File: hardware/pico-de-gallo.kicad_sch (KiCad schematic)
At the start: 12 parts, among them J1 Conn_02x08_Odd_Even, J2 Conn_01x02, J3 Conn_01x04, J4 Conn_01x05, J5 Conn_01x02, J6 Conn_01x03, J7 Conn_02x05_Odd_Even

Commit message: Minor updates
Signed-off-by: Felipe Balbi <febalbi@microsoft.com>
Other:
- company: (none) -> ${COMPANY}
- title: (none) -> ${PROJECT}
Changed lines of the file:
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@@
 	(generator "eeschema")
 	(generator_version "9.0")
-	(paper "A4")
+	(paper "USLetter")
+	(title_block
+		(title "${PROJECT}")
+		(date "2025-08-29")
+		(rev "${REVISION}")
+		(company "${COMPANY}")
+		(comment 1 "Designed by: ${AUTHOR}")
+		(comment 2 "https://creativecommons.org/licenses/by-sa/4.0/")
+		(comment 3 "Attribution Share-Alike 4.0 License")
+		(comment 4 "Released under the Creative Commons")
+	)
 	(no_connect
 		(at 146.05 57.15)

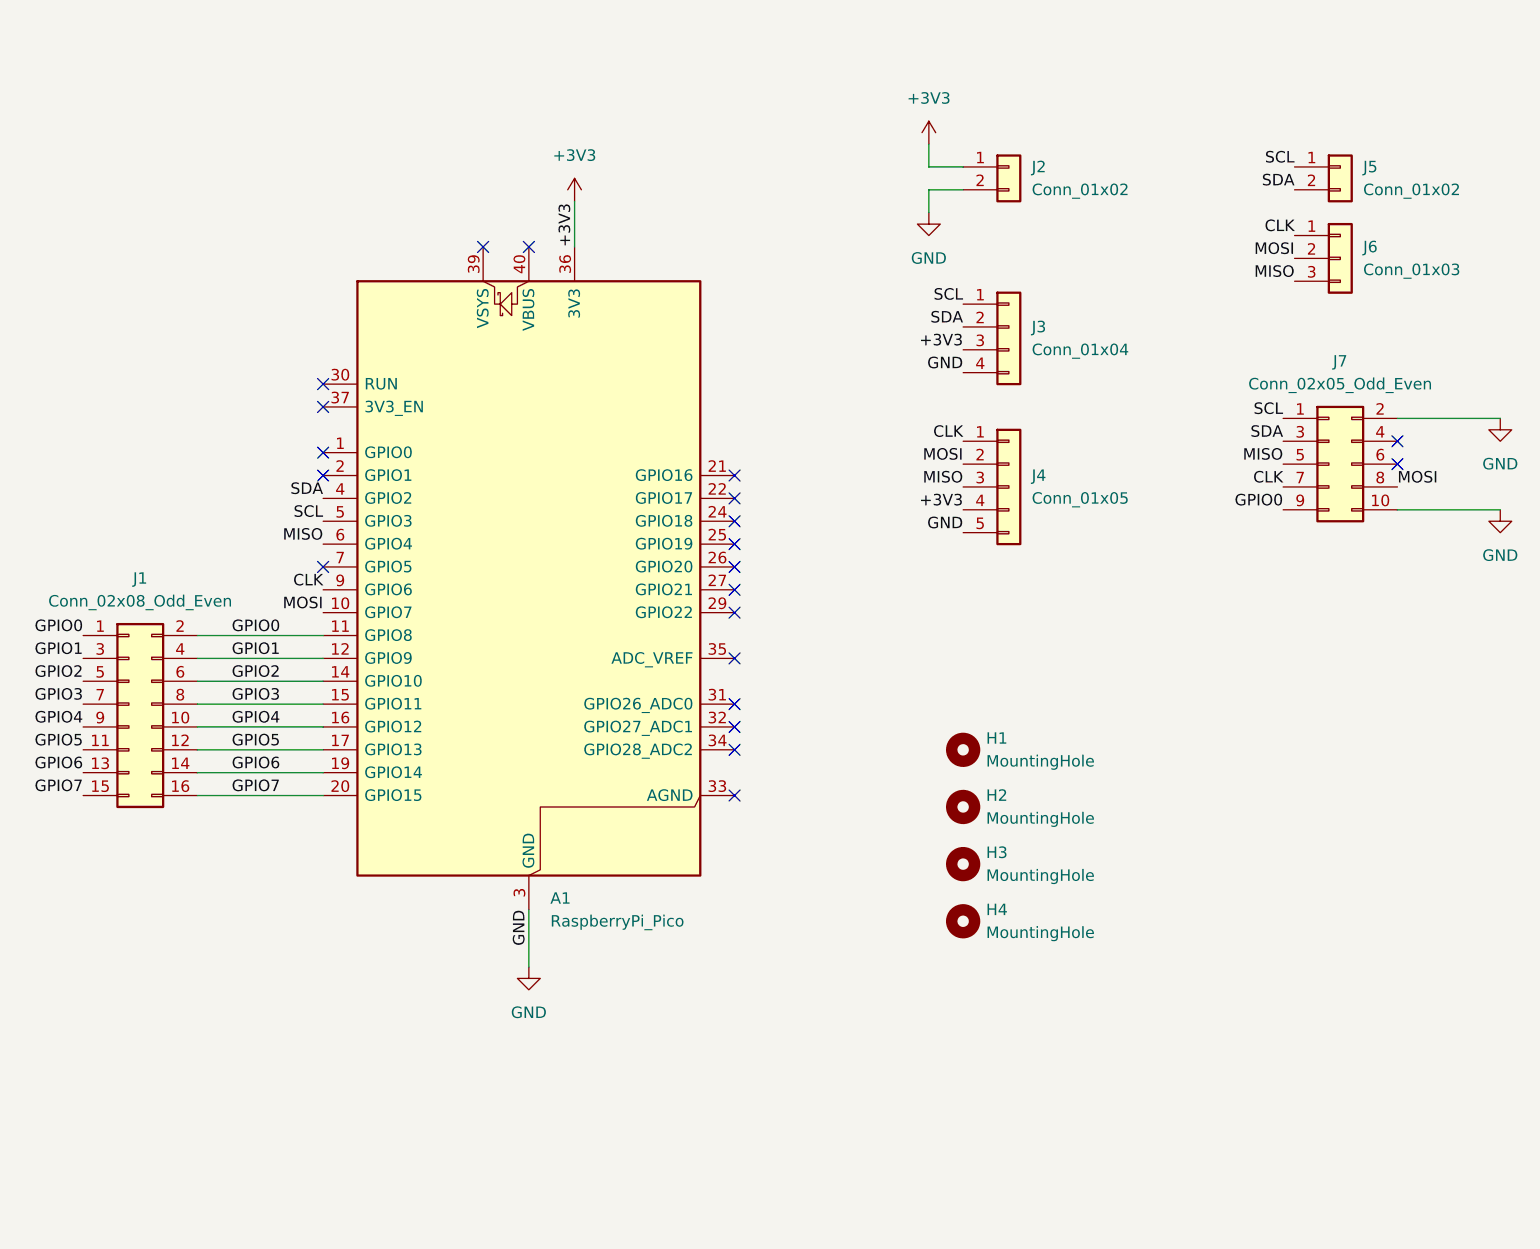
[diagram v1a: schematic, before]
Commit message: Pico de Gallo Hardware v1.1
Update the PCB for revision 1.1 of the main board.
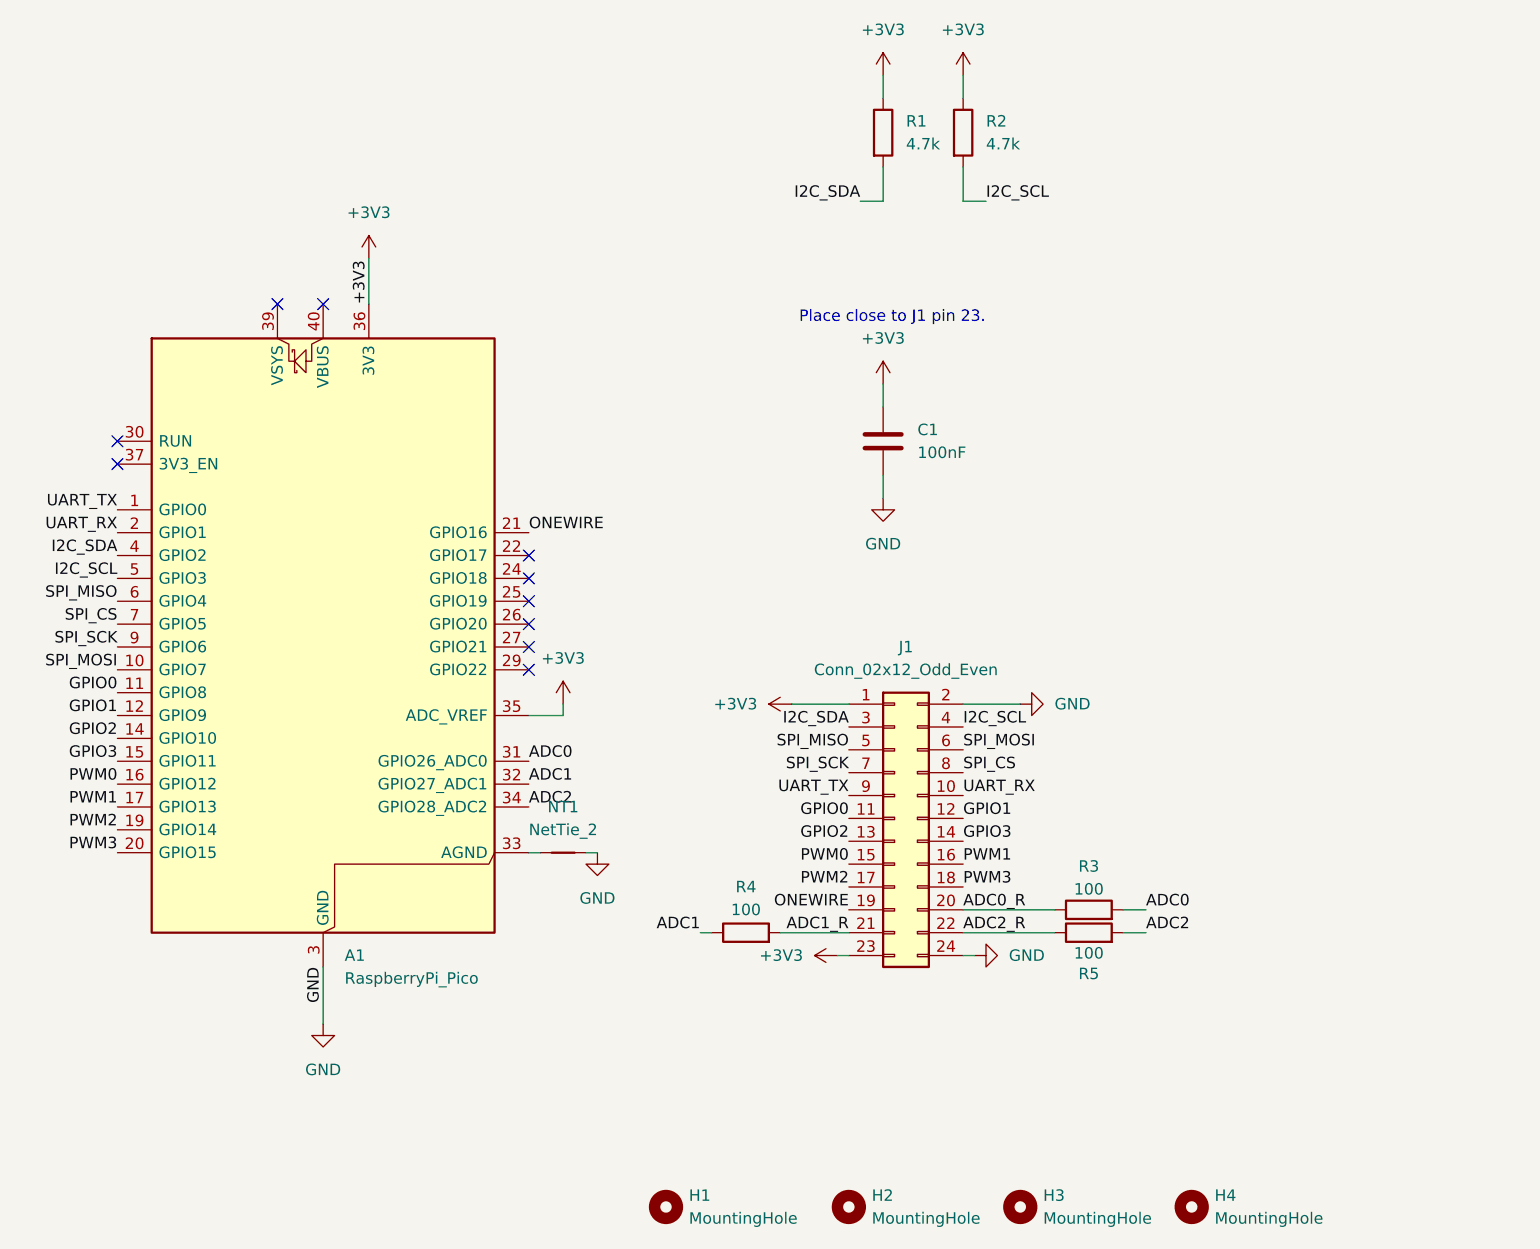
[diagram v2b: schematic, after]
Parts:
- removed J1: Conn_02x08_Odd_Even, Connector_PinHeader_2.54mm:PinHeader_2x08_P2.54mm_Vertical, symbol Connector_Generic:Conn_02x08_Odd_Even
- removed J2, J5: Conn_01x02, Connector_PinHeader_2.54mm:PinHeader_1x02_P2.54mm_Vertical, symbol Connector_Generic:Conn_01x02
- removed J3: Conn_01x04, Connector_PinSocket_2.54mm:PinSocket_1x04_P2.54mm_Horizontal, symbol Connector_Generic:Conn_01x04
- removed J4: Conn_01x05, Connector_PinSocket_2.54mm:PinSocket_1x05_P2.54mm_Horizontal, symbol Connector_Generic:Conn_01x05
- removed J6: Conn_01x03, Connector_PinHeader_2.54mm:PinHeader_1x03_P2.54mm_Vertical, symbol Connector_Generic:Conn_01x03
- removed J7: Conn_02x05_Odd_Even, Connector_PinHeader_2.54mm:PinHeader_2x05_P2.54mm_Vertical_SMD, symbol Connector_Generic:Conn_02x05_Odd_Even
- added C1: 100nF, Capacitor_SMD:C_0603_1608Metric_Pad1.08x0.95mm_HandSolder, symbol Device:C
- added J1: Conn_02x12_Odd_Even, Connector_IDC:IDC-Header_2x12_P2.54mm_Vertical, symbol Connector_Generic:Conn_02x12_Odd_Even
- added NT1: NetTie_2, NetTie:NetTie-2_SMD_Pad0.5mm, symbol Device:NetTie_2
- added R1, R2: 4.7k, Resistor_SMD:R_0603_1608Metric_Pad0.98x0.95mm_HandSolder, symbol Device:R
- added R3, R4, R5: 100, Resistor_SMD:R_0603_1608Metric_Pad0.98x0.95mm_HandSolder, symbol Device:R
- A1: now left out of the parts list
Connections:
- net +3V3: now also A1.35 (ADC_VREF), C1.1, J1.1 (Pin_1), J1.23 (Pin_23), R1.1, R2.1
- net GND: now also C1.2, J1.2 (Pin_2), J1.24 (Pin_24), NT1.2
- net GPIO0: now also J1.11 (Pin_11)
- net GPIO1: now also J1.12 (Pin_12)
- net GPIO2: now also J1.13 (Pin_13)
- net GPIO3: now also J1.14 (Pin_14)
- net UART_TX: now reaches A1.1 (GPIO0)
- net UART_TX: now also J1.9 (Pin_9)
- net UART_RX: now reaches A1.2 (GPIO1)
- net UART_RX: now also J1.10 (Pin_10)
- net ONEWIRE: now reaches A1.21 (GPIO16)
- net ONEWIRE: now also J1.19 (Pin_19)
- net ADC0: now reaches A1.31 (GPIO26_ADC0)
- net ADC0: now also R3.2
- net ADC1: now reaches A1.32 (GPIO27_ADC1)
- net ADC1: now also R4.1
- net at A1.33 (AGND): now also NT1.1
- net ADC2: now reaches A1.34 (GPIO28_ADC2)
- net ADC2: now also R5.2
- net SPI_CS: now reaches A1.7 (GPIO5)
- net SPI_CS: now also J1.8 (Pin_8)
- net CLK renamed SPI_SCK
- net SPI_SCK: now also J1.7 (Pin_7)
- net GPIO4 renamed PWM0
- net PWM0: now also J1.15 (Pin_15)
- net GPIO5 renamed PWM1
- net PWM1: now also J1.16 (Pin_16)
- net GPIO6 renamed PWM2
- net PWM2: now also J1.17 (Pin_17)
- net GPIO7 renamed PWM3
- net PWM3: now also J1.18 (Pin_18)
- net MISO renamed SPI_MISO
- net SPI_MISO: now also J1.5 (Pin_5)
- net MOSI renamed SPI_MOSI
- net SPI_MOSI: now also J1.6 (Pin_6)
- net SCL renamed I2C_SCL
- net I2C_SCL: now also J1.4 (Pin_4), R2.2
- net SDA renamed I2C_SDA
- net I2C_SDA: now also J1.3 (Pin_3), R1.2
- new net ADC0_R: J1.20 (Pin_20), R3.1
- new net ADC1_R: J1.21 (Pin_21), R4.2
- new net ADC2_R: J1.22 (Pin_22), R5.1
- no-connect marks 21 -> 10
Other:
- note added: "Place close to J1 pin 23."
- moved on the sheet: A1, H1, H2, H3, H4

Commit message: add Pico2 LCSC part number
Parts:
- A1: LCSC (none) -> C41407547; now in the parts list
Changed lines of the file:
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@@
 		(body_style 1)
 		(exclude_from_sim no)
-		(in_bom no)
+		(in_bom yes)
 		(on_board yes)
-		(in_pos_files no)
+		(in_pos_files yes)
 		(dnp no)
 		(fields_autoplaced yes)
@@
 			(hide yes)
 			(show_name no)
+			(do_not_autoplace no)
+			(effects
+				(font
+					(size 1.27 1.27)
+				)
+			)
+		)
+		(property "LCSC" "C41407547"
+			(at 123.19 101.6 0)
+			(hide yes)
+			(show_name no)

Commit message: Fix JLCPCB part number
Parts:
- J1: LCSC C9129 -> C9137
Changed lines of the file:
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@@
 			)
 		)
-		(property "LCSC" "C9129"
+		(property "LCSC" "C9137"
 			(at 186.69 120.65 0)
 			(hide yes)
